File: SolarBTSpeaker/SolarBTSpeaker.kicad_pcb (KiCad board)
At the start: 2 copper layers, 92 parts, among them J1 Conn_01x01, J10 OUT_LEFT-, J11 IN_LEFT+, J12 IN_LEFT-, J13 OUT_RIGHT-, J14 IN_RIGHT-, J15 OUT_RIGHT+, J16 IN_RIGHT+, J17 GAIN_Jumper, J2 Conn_01x01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

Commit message: PCB and schematic significantly updated
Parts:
- J1: value Conn_01x01 -> BAT+
- J10: value OUT_LEFT- -> OUTL-
- J11: value IN_LEFT+ -> LIN+
- J12: value IN_LEFT- -> LIN-
- J13: value OUT_RIGHT- -> OUTR-
- J14: value IN_RIGHT- -> RIN-
- J15: value OUT_RIGHT+ -> OUTR+
- J16: value IN_RIGHT+ -> RIN+
- J2: value Conn_01x01 -> BAT-
- J3: value Conn_01x01 -> SlrPnl+
- J4: value Conn_01x01 -> SlrPnl-
- J5: value Conn_01x01 -> USB+
- J6: value Conn_01x01 -> USB-
- J7, J8: value Conn_01x01 -> ThmCpl
- J9: value OUT_LEFT+ -> OUTL+
- SW1: value SW_Input -> SW_Power
- SW2: value SW_SPDT -> SW_AMP
- TP1: value TestPoint -> VBUS; footprint TestPoint:TestPoint_Pad_D1.0mm -> TestPoint:TestPoint_Pad_D1.5mm
- TP2: value TestPoint -> BAT; footprint TestPoint:TestPoint_Pad_D1.0mm -> TestPoint:TestPoint_Pad_D1.5mm
- TP3: value TestPoint -> COUT; footprint TestPoint:TestPoint_Pad_D1.0mm -> TestPoint:TestPoint_Pad_D1.5mm
- TP4: value TestPoint -> DOUT; footprint TestPoint:TestPoint_Pad_D1.0mm -> TestPoint:TestPoint_Pad_D1.5mm
- TP5: value TestPoint -> 12V; footprint TestPoint:TestPoint_Pad_D1.0mm -> TestPoint:TestPoint_Pad_D1.5mm
- TP6: value TestPoint -> EXT; footprint TestPoint:TestPoint_Pad_D1.0mm -> TestPoint:TestPoint_Pad_D1.5mm
- moved TP3 155.6 mm to (88.9, 86.4)
- moved R4 137.7 mm to (93.9, 58.4), turned to 90 degrees
- moved Rth1 134.4 mm to (93.0, 63.8), turned to 270 degrees
- moved R1 124.1 mm to (96.5, 73.7), turned to 180 degrees
- moved R6 123.6 mm to (88.9, 82.5), turned to 90 degrees
- moved R5 117.5 mm to (110.7, 63.8)
- moved U1 114.8 mm to (96.4, 63.9), turned to 270 degrees
- moved TP5 111.9 mm to (140.0, 51.3)
- moved J1 111.8 mm to (108.0, 76.7)
- moved TP1 109.6 mm to (100.2, 61.3), turned to 270 degrees
- moved R8 108.0 mm to (92.2, 76.2), turned to 270 degrees
- moved R3 108.0 mm to (92.2, 79.5), turned to 180 degrees
- moved TP6 104.8 mm to (136.9, 64.8)
- moved R2 103.9 mm to (101.1, 80.3)
- moved C2 101.6 mm to (96.6, 56.9), turned to 180 degrees
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- renumbered Rtherm1 to Rth1
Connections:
- TP2 pad 1: GND -> BAT+
- TP3 pad 1: BAT+ -> Net-(R6-Pad1)
- TP4 pad 1: 12V -> Net-(R2-Pad1)
- TP6 pad 1: 12V -> Net-(TP6-Pad1)
- U5 pad 4: Net-(U5-Pad4) -> Net-(TP6-Pad1)
- U6 pad 1: Net-(U5-Pad4) -> Net-(TP6-Pad1)
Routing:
- net 12V: track 0.00 -> 153.2 mm, vias 0 -> 1
- net BAT+: track 0.00 -> 46.2 mm, vias 0 -> 2
- net Net-(D4-Pad2): track 0.00 -> 29.3 mm
- net Net-(C1-Pad2): track 0.00 -> 21.8 mm
- net Net-(C2-Pad1): track 0.00 -> 18.2 mm
- net Net-(C8-Pad1): track 0.00 -> 18.1 mm
- net Net-(R2-Pad1): track 0.00 -> 17.1 mm, vias 0 -> 2
- net Net-(U3-Pad3): track 0.00 -> 15.1 mm
- net VDPM: track 0.00 -> 14.6 mm, vias 0 -> 1
- net Net-(R6-Pad1): track 0.00 -> 13.3 mm, vias 0 -> 2
- net Net-(TP6-Pad1): track 0.00 -> 12.9 mm, vias 0 -> 2
- net Net-(Rsense1-Pad1): track 0.00 -> 11.2 mm
- net Net-(D2-Pad1): track 0.00 -> 10.4 mm, vias 0 -> 1
- net Net-(J17-Pad2): track 0.00 -> 10.4 mm, vias 0 -> 1
- net Net-(C34-Pad1): track 0.00 -> 10.0 mm
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
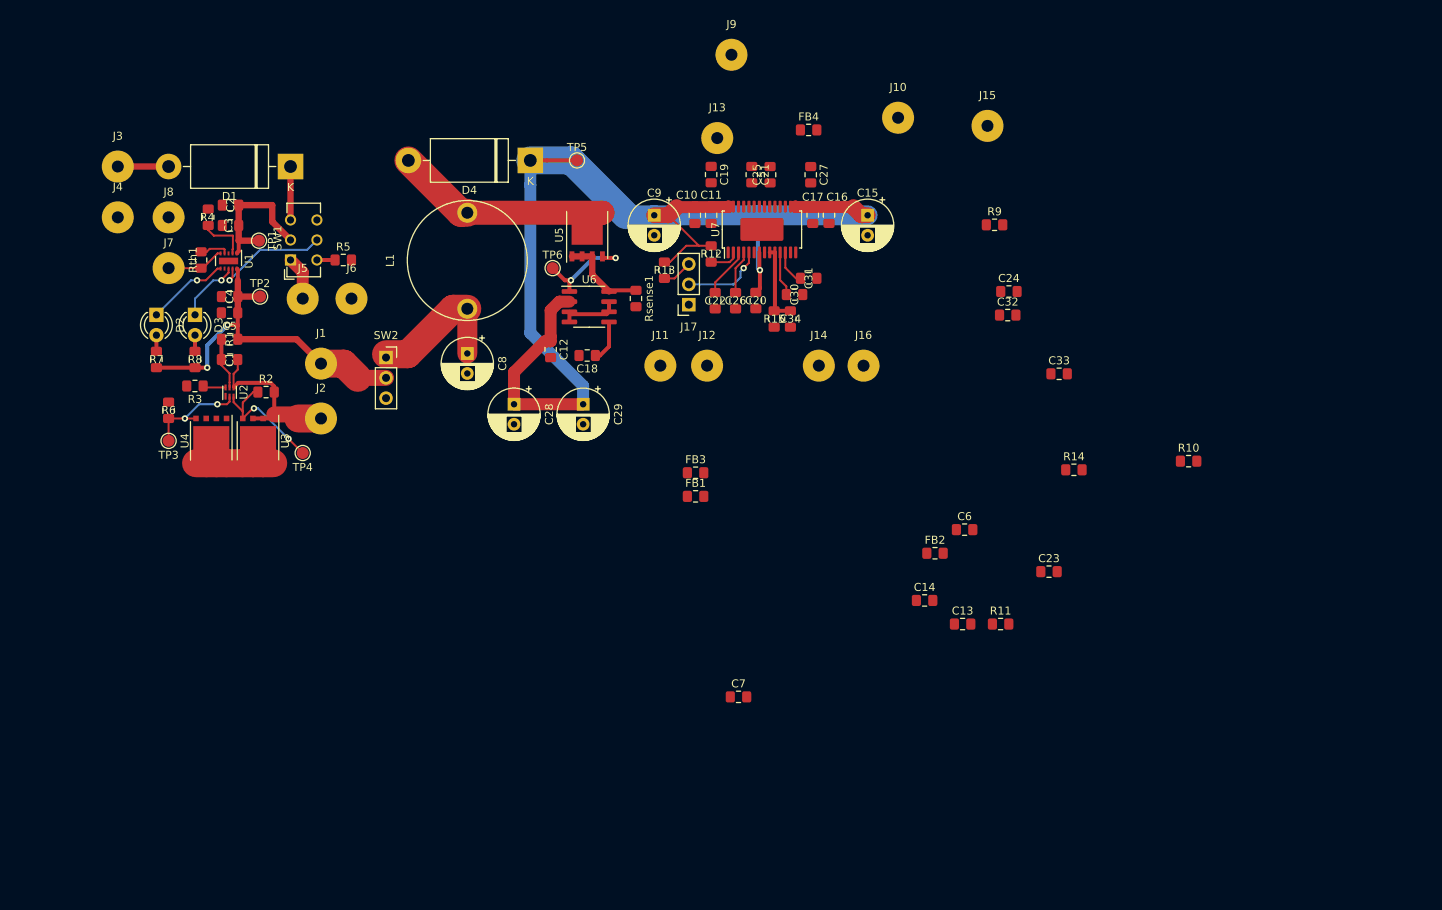
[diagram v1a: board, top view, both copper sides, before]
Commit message: PCB updated, ground fills added
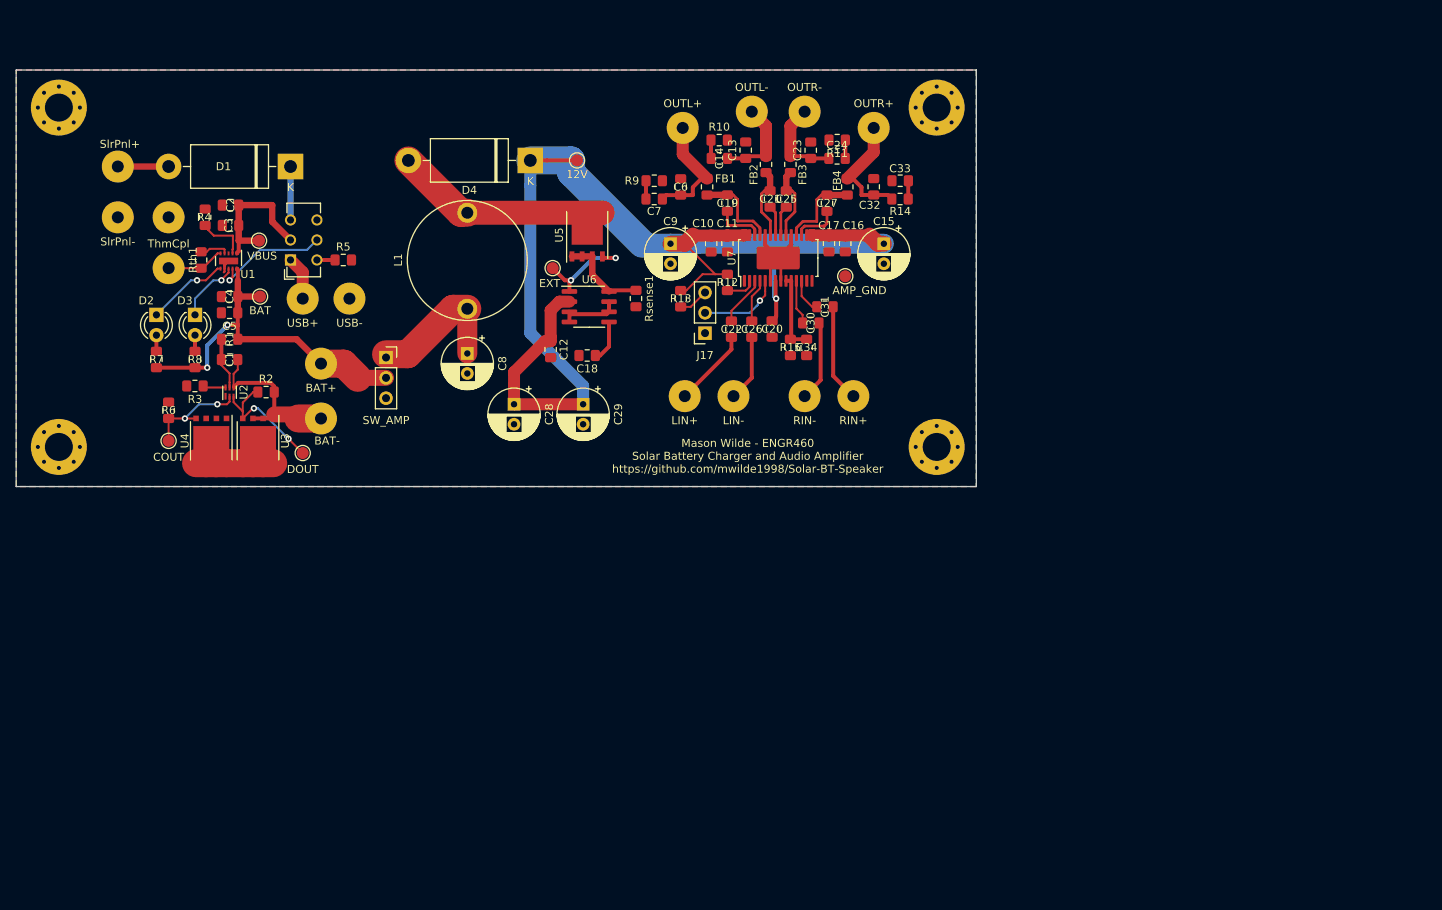
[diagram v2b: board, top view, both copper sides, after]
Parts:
- added REF**: MountingHole_3.5mm_Pad_Via, MountingHole:MountingHole_3.5mm_Pad_Via, F.Cu at (184.9, 44.7)
- added REF**: MountingHole_3.5mm_Pad_Via, MountingHole:MountingHole_3.5mm_Pad_Via, F.Cu at (184.9, 87.1)
- added REF**: MountingHole_3.5mm_Pad_Via, MountingHole:MountingHole_3.5mm_Pad_Via, F.Cu at (75.2, 87.1)
- added REF**: MountingHole_3.5mm_Pad_Via, MountingHole:MountingHole_3.5mm_Pad_Via, F.Cu at (75.2, 44.7)
- added TP7: AMP_GND, TestPoint:TestPoint_Pad_D1.5mm, F.Cu at (173.5, 65.8)
- moved R10 71.1 mm to (157.7, 48.8)
- moved C13 65.1 mm to (161.0, 50.0), turned to 90 degrees
- moved R11 63.8 mm to (172.5, 48.8), turned to 180 degrees
- moved C7 63.1 mm to (149.6, 56.1), turned to 180 degrees
- moved C14 60.9 mm to (157.7, 51.1), turned to 180 degrees
- moved C23 60.5 mm to (169.2, 50.0), turned to 90 degrees
- moved C6 55.6 mm to (152.9, 54.6), turned to 90 degrees
- moved FB2 53.0 mm to (163.6, 51.8), turned to 270 degrees
- moved R9 42.9 mm to (149.6, 53.8)
- moved R14 42.2 mm to (180.3, 53.8), turned to 180 degrees
- moved FB3 40.3 mm to (166.6, 51.8), turned to 270 degrees
- moved FB1 38.7 mm to (156.2, 54.6), turned to 270 degrees
- moved C33 29.5 mm to (180.3, 56.1)
- moved C24 27.2 mm to (172.5, 51.1)
- moved C32 23.2 mm to (177.0, 54.6), turned to 90 degrees
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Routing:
- net GND: track 7.74 -> 22.8 mm
- net Net-(C32-Pad1): track 0.00 -> 14.9 mm
- net Net-(C6-Pad1): track 0.00 -> 14.8 mm
- net Net-(C31-Pad2): track 0.00 -> 12.2 mm
- net Net-(C23-Pad1): track 0.00 -> 11.2 mm
- net Net-(C13-Pad1): track 0.00 -> 11.2 mm
- net Net-(C19-Pad1): track 0.00 -> 10.8 mm
- net Net-(C27-Pad1): track 0.00 -> 10.6 mm
- net Net-(C30-Pad2): track 0.00 -> 10.1 mm
- net Net-(C22-Pad2): track 0.00 -> 9.77 mm
- net Net-(C21-Pad1): track 0.00 -> 9.33 mm
- net Net-(C25-Pad1): track 0.00 -> 9.33 mm
- net Net-(C26-Pad2): track 0.00 -> 8.29 mm
- net Net-(C19-Pad2): track 0.00 -> 6.15 mm
- net Net-(C27-Pad2): track 0.00 -> 5.77 mm
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- added copper zone on B.Cu, net GND
- added copper zone on F.Cu, net GND
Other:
- board outline added: 120 x 52.1 mm
- board text added: "Mason Wilde - ENGR460 Solar Battery Charger and Audio Amplifier https://github.com/mwilde1998/Solar-BT-Speaker"

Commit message: Schematic and PCB finalized, gerbers and drill plot created
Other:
- board text added: "Mason Wilde - ENGR460 - v1.0 Solar Battery Charger and Audio Amplifier https://github.com/mwilde1998/Solar-BT-Speaker"
- board text removed: "Mason Wilde - ENGR460 Solar Battery Charger and Audio Amplifier https://github.com/mwilde1998/Solar-BT-Speaker"
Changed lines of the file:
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@@
       (usegerberadvancedattributes false)
       (creategerberjobfile false)
-      (excludeedgelayer true)
-      (linewidth 0.100000)
+      (excludeedgelayer false)
+      (linewidth 0.150000)
       (plotframeref false)
       (viasonmask false)
       (mode 1)
-      (useauxorigin false)
+      (useauxorigin true)
       (hpglpennumber 1)
       (hpglpenspeed 20)
@@
       (outputformat 1)
       (mirror false)
-      (drillshape 1)
+      (drillshape 0)
       (scaleselection 1)
-      (outputdirectory ""))
+      (outputdirectory "Gerbers/"))
   )
   (net 0 "")
@@
       (net 4 GND))
   )
-  (gr_text "Mason Wilde - ENGR460\nSolar Battery Charger and Audio Amplifier\nhttps://github.com/mwilde1998/Solar-BT-Speaker" (at 161.29 88.265) (layer F.SilkS)
+  (gr_text "Mason Wilde - ENGR460 - v1.0\nSolar Battery Charger and Audio Amplifier\nhttps://github.com/mwilde1998/Solar-BT-Speaker" (at 161.29 88.265) (layer F.SilkS)
     (effects (font (size 1 1) (thickness 0.25)))
   )

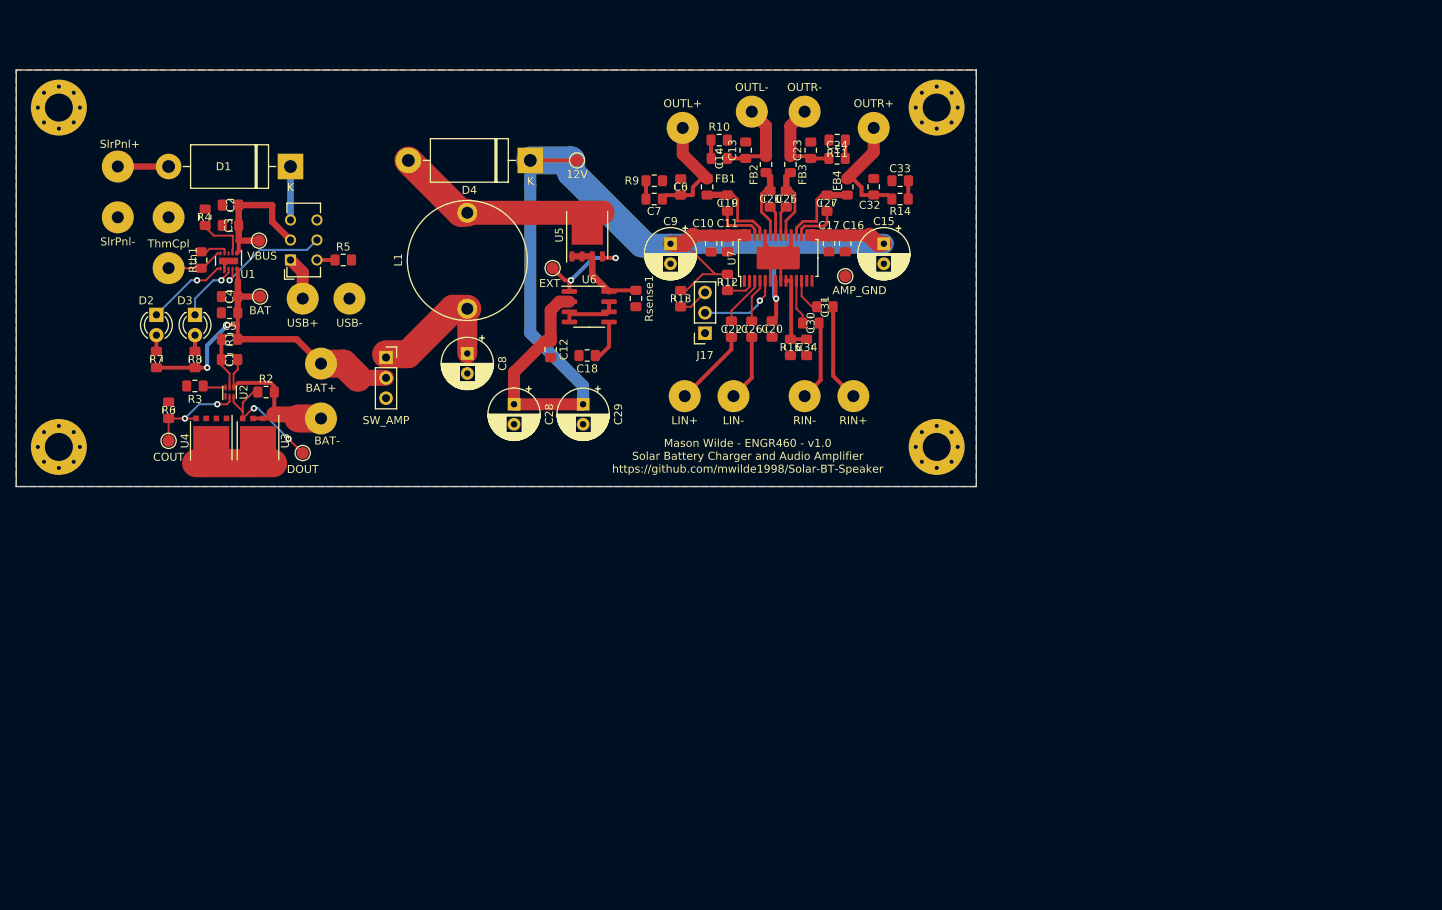
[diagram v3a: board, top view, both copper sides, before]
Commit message: PCB, schematic, and silkscreen references finalized
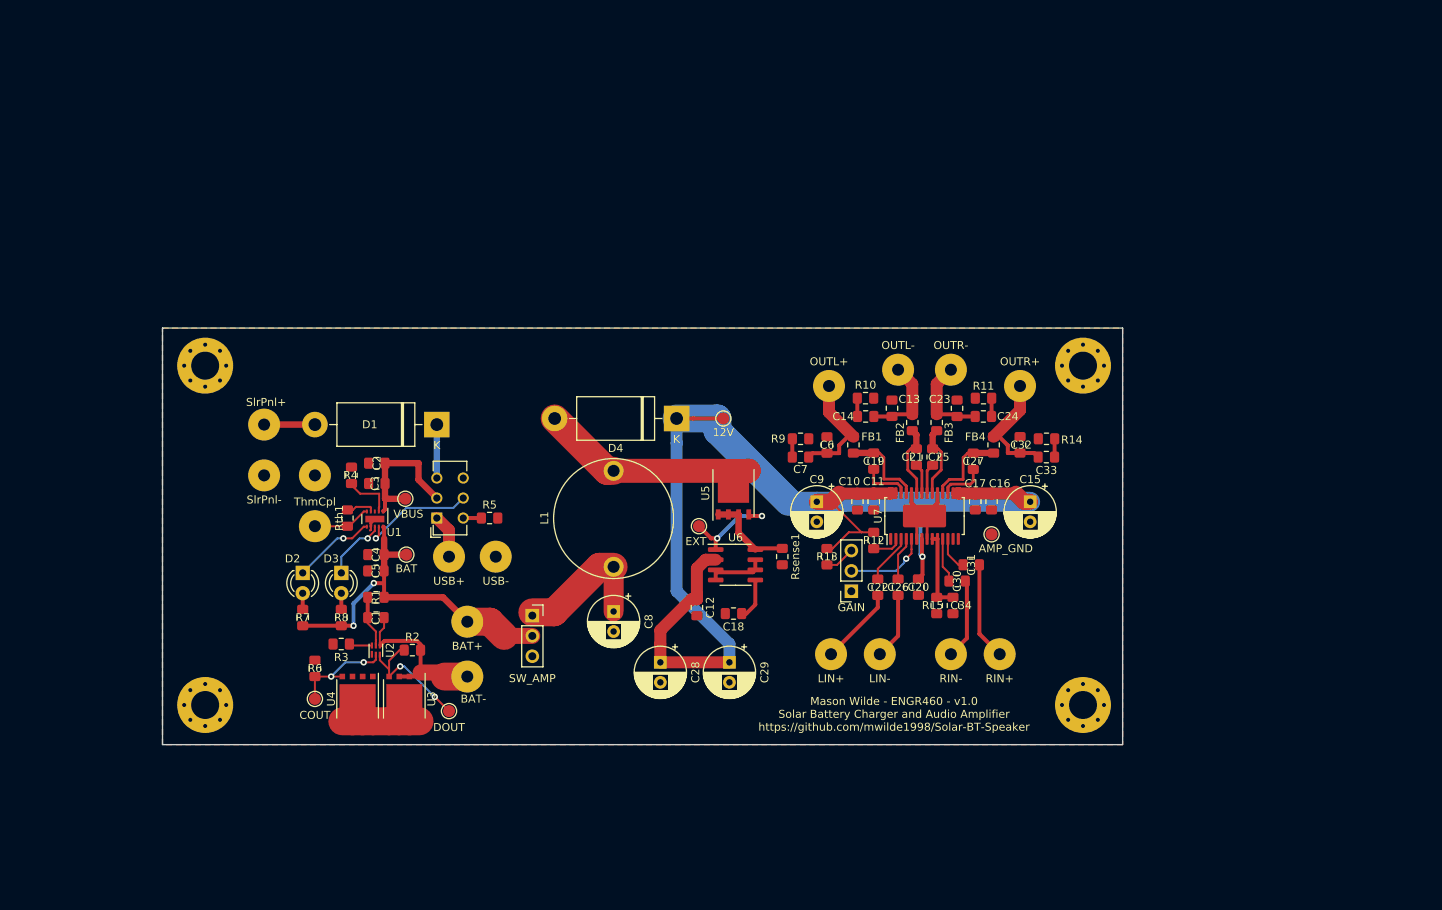
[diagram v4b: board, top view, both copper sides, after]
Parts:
- J17: value GAIN_Jumper -> GAIN
- moved C12 37.1 mm to (154.9, 107.2)
- moved C18 37.1 mm to (159.5, 108.0)
- moved C23 37.1 mm to (187.5, 82.3)
- moved J17 37.1 mm to (174.2, 105.2)
- moved L1 37.1 mm to (144.5, 102.1)
- moved U2 37.1 mm to (114.8, 112.5)
- moved C10 37.1 mm to (175.0, 94.0)
- moved C11 37.1 mm to (177.0, 94.0)
- moved C13 37.1 mm to (179.3, 82.3)
- moved C15 37.1 mm to (196.6, 94.0)
- moved C16 37.1 mm to (191.8, 94.0)
- moved C17 37.1 mm to (189.7, 94.0)
- moved C19 37.1 mm to (177.0, 88.9)
- moved C27 37.1 mm to (189.5, 88.9)
- moved D4 37.1 mm to (152.4, 83.6)
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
